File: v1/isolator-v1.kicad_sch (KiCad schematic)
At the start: 43 parts, among them J1 HOST, J2 PORT, Q1 2N7002, T1 750313638, U1 ADuM4165, U2 USBLC6-2SC6, U3 USBLC6-2SC6, U4 SN6505BDBV, U5 TLV76750DGNR, U6 TPS2553DBV, Y1 24M 8pF

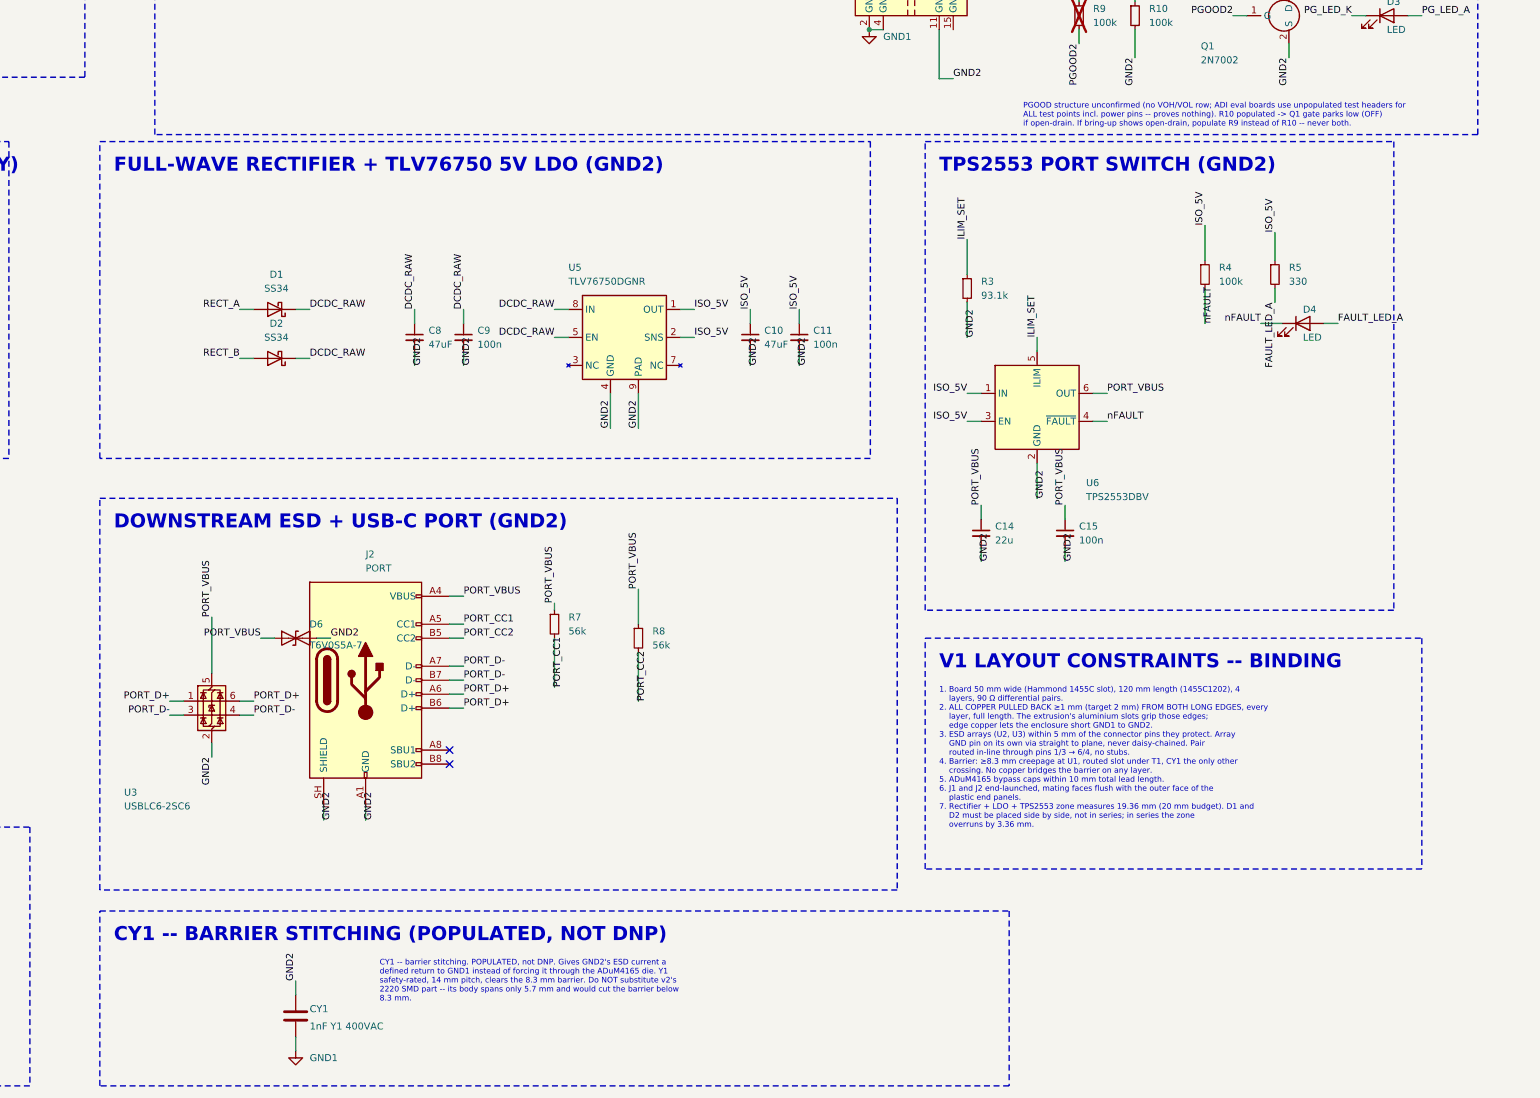
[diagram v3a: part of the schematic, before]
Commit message: fix(v1): final whole-branch review fix wave — R3/FAULT docs, ADuM4165 GND-pin bypass trap, VBUS_HOST cap placement, PGOOD push-pull, title block
Applies all findings from the final whole-branch review
(docs/superpowers/reviews/2026-07-28-v1-schematic-review.md, "Fix round 2"):

Important:
- Corrects the spec's power-budget claim about R3/TPS2553 ILIM. R3 is kept
  unchanged (93.1 kOhm); the documentation now states I_OS = 252/286/324 mA
  min/nom/max (SLVS841F Eq. 1), that the DC-DC's own ~240 mA droop -- not the
  TPS2553 -- is the real port ceiling, that R3's job is soft-start plus a
  short-circuit backstop, and that FAULT will not light on a normal overload
  as an accepted consequence. Mirrored into the spec's verification plan and
  the review record's bring-up notes.
- Adds a new binding layout-constraint item: ADuM4165 U1 pins 4, 7 (GND1)
  and 15, 16, 17 (GND2) are ground-only and not suitable for bypass
  capacitance (datasheet Table 12, p.12); bypass returns must use pins
  2/10 (GND1) or 11/19 (GND2) instead.
- Gives C3, C4, C6, C7 (all on VBUS_HOST) specific Description properties
  naming which IC each bypasses and where it must be placed, verified
  against the SN6505B datasheet (Table 5-1, Sec 10) and the ADuM4165's own
  10 mm bypass-lead budget; adds a matching layout-constraint item.

Minor:
- Reconciles the spec's two DCDC_RAW figures (6.15 V unloaded vs. ~5.8 V
  full load).
- Notes 85% converter efficiency drops the port figure to ~226 mA; 240 mA
  is documented as a best case, not a floor.
- Adds a VDD2-only pull-up warning to the PGOOD schematic note, citing
  PGOOD's VDD2 + 0.5 V absolute maximum (Table 8, p.10).
- Fills in the previously-empty title block (title, date, rev). No
  company/author precedent exists in either project, so those stay blank.

Also records that PGOOD is confirmed push-pull (Table 18, p.15) in both the
review record and the schematic note. R10 stays populated and R9 stays DNP,
unchanged; R10 removal is recorded as an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
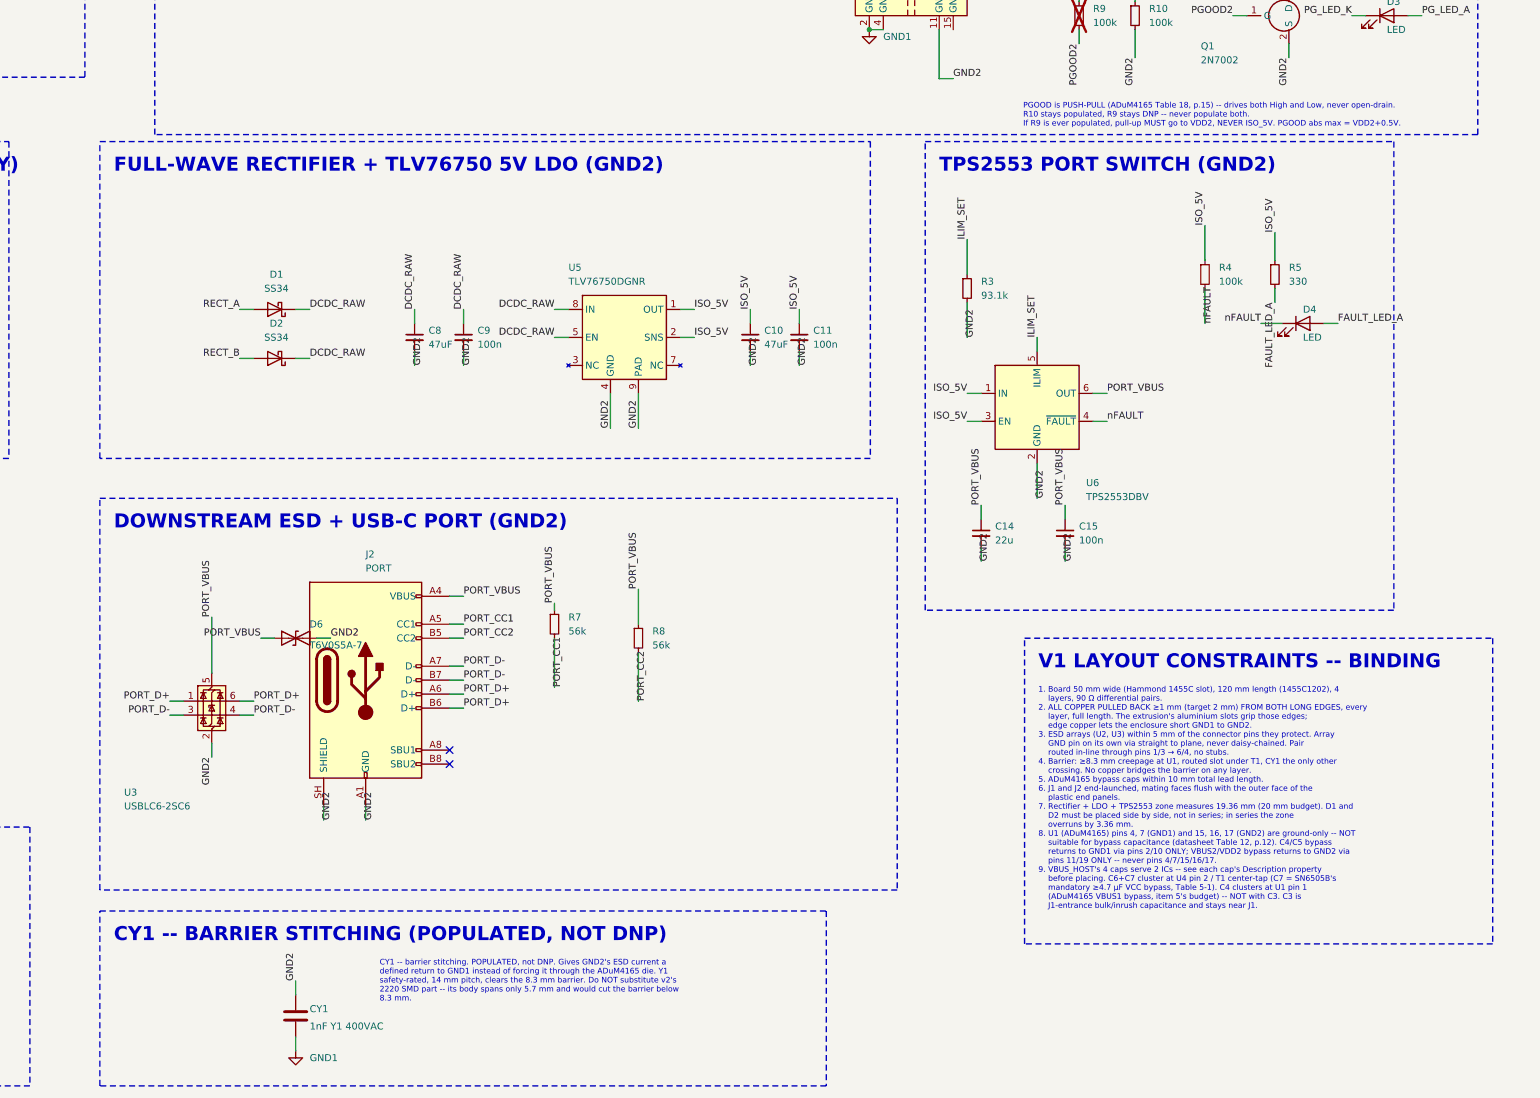
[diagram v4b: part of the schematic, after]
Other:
- note added: "PGOOD is PUSH-PULL (ADuM4165 Table 18, p.15) -- drives both High and Low, never open-drain. R10 stays populated, R9 stays DNP -- never populate both. If R9 is ever populated, pull-up MUST go to VDD2, NEVER ISO_5V. PGOOD abs max = VDD2+0.5V."
- note removed: "PGOOD structure unconfirmed (no VOH/VOL row; ADI eval boards use unpopulated test headers for ALL test points incl. power pins -- proves nothing). R10 populated -> Q1 gate parks low (OFF) if open-drain. If bring-up shows open-drain, populate R9 instead of R10 -- never both."
- title: (none) -> Isolated USB 2.0 Cable — v1
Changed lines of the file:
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@@
 	(generator_version "10.0")
 	(paper "A3")
+	(title_block
+		(title "Isolated USB 2.0 Cable — v1")
+		(date "2026-07-30")
+		(rev "v1.0")
+	)
 	(symbol
 		(lib_id "Device:D_TVS")
@@
 			)
 		)
-		(property "Description" "Unpolarized capacitor, small symbol"
+		(property "Description" "VBUS_HOST bulk/inrush cap at J1 entrance (SN6505B Sec 9.2.2.4 permits supply-entrance placement on a 4-layer board). NOT the SN6505B VCC bypass -- see C7. Layout: place near J1."
 			(at 25.4 49.53 0)
 			(hide yes)
@@
 			)
 		)
-		(property "Description" "Unpolarized capacitor, small symbol"
+		(property "Description" "ADuM4165 U1 VBUS1 mandatory 0.1uF bypass to GND1 (datasheet Table 12, pin 1). Layout: MUST cluster within U1's 10 mm bypass-lead budget at U1 pin 1 -- do NOT leave with C3 near J1."
 			(at 40.64 49.53 0)
 			(hide yes)
@@
 			)
 		)
-		(property "Description" "Unpolarized capacitor, small symbol"
+		(property "Description" "SN6505B U4 VCC close-to-pin bypass, 0.1uF (datasheet Sec 10, Power Supply Recommendations). Layout: place immediately at U4 pin 2 / T1 center-tap, alongside C7."
 			(at 25.4 130.81 0)
 		(hide yes)
@@
 			)
 		)
-		(property "Description" "Unpolarized capacitor, small symbol"
+		(property "Description" "SN6505B U4 VCC mandatory bypass, >=4.7uF low-ESR (datasheet Table 5-1). Layout: place close to U4 pin 2 / T1 center-tap, NOT near J1."
 			(at 38.1 130.81 0)
 		(hide yes)
@@
 		)
 	)
-	(text "PGOOD structure unconfirmed (no VOH/VOL row; ADI eval boards use unpopulated test headers for\nALL test points incl. power pins -- proves nothing). R10 populated -> Q1 gate parks low (OFF)\nif open-drain. If bring-up shows open-drain, populate R9 instead of R10 -- never both."
+	(text "PGOOD is PUSH-PULL (ADuM4165 Table 18, p.15) -- drives both High and Low, never open-drain.\nR10 stays populated, R9 stays DNP -- never populate both.\nIf R9 is ever populated, pull-up MUST go to VDD2, NEVER ISO_5V. PGOOD abs max = VDD2+0.5V."
 		(exclude_from_sim no)
 		(at 332.74 97.79 0)
@@
 	(rectangle
 		(start 165.1 240.03)
-		(end 330.2 271.78)
+		(end 297.0 271.78)
 		(stroke
 			(width 0.254)
@@
 	)
 	(rectangle
-		(start 314.96 190.5)
-		(end 405.13 232.41)
+		(start 333.0 190.5)
+		(end 418.0 246.0)
 		(stroke
 			(width 0.254)
@@
 	(text "V1 LAYOUT CONSTRAINTS -- BINDING"
 		(exclude_from_sim no)
-		(at 317.5 196.34 0)
+		(at 335.5 196.34 0)
 		(effects
 			(font
@@
 		)
 	)
-	(text "1. Board 50 mm wide (Hammond 1455C slot), 120 mm length (1455C1202), 4\n    layers, 90 Ω differential pairs.\n2. ALL COPPER PULLED BACK ≥1 mm (target 2 mm) FROM BOTH LONG EDGES, every\n    layer, full length. The extrusion's aluminium slots grip those edges;\n    edge copper lets the enclosure short GND1 to GND2.\n3. ESD arrays (U2, U3) within 5 mm of the connector pins they protect. Array\n    GND pin on its own via straight to plane, never daisy-chained. Pair\n    routed in-line through pins 1/3 → 6/4, no stubs.\n4. Barrier: ≥8.3 mm creepage at U1, routed slot under T1, CY1 the only other\n    crossing. No copper bridges the barrier on any layer.\n5. ADuM4165 bypass caps within 10 mm total lead length.\n6. J1 and J2 end-launched, mating faces flush with the outer face of the\n    plastic end panels.\n7. Rectifier + LDO + TPS2553 zone measures 19.36 mm (20 mm budget). D1 and\n    D2 must be placed side by side, not in series; in series the zone\n    overruns by 3.36 mm."
+	(text "1. Board 50 mm wide (Hammond 1455C slot), 120 mm length (1455C1202), 4\n    layers, 90 Ω differential pairs.\n2. ALL COPPER PULLED BACK ≥1 mm (target 2 mm) FROM BOTH LONG EDGES, every\n    layer, full length. The extrusion's aluminium slots grip those edges;\n    edge copper lets the enclosure short GND1 to GND2.\n3. ESD arrays (U2, U3) within 5 mm of the connector pins they protect. Array\n    GND pin on its own via straight to plane, never daisy-chained. Pair\n    routed in-line through pins 1/3 → 6/4, no stubs.\n4. Barrier: ≥8.3 mm creepage at U1, routed slot under T1, CY1 the only other\n    crossing. No copper bridges the barrier on any layer.\n5. ADuM4165 bypass caps within 10 mm total lead length.\n6. J1 and J2 end-launched, mating faces flush with the outer face of the\n    plastic end panels.\n7. Rectifier + LDO + TPS2553 zone measures 19.36 mm (20 mm budget). D1 and\n    D2 must be placed side by side, not in series; in series the zone\n    overruns by 3.36 mm.\n8. U1 (ADuM4165) pins 4, 7 (GND1) and 15, 16, 17 (GND2) are ground-only -- NOT\n    suitable for bypass capacitance (datasheet Table 12, p.12). C4/C5 bypass\n    returns to GND1 via pins 2/10 ONLY; VBUS2/VDD2 bypass returns to GND2 via\n    pins 11/19 ONLY -- never pins 4/7/15/16/17.\n9. VBUS_HOST's 4 caps serve 2 ICs -- see each cap's Description property\n    before placing. C6+C7 cluster at U4 pin 2 / T1 center-tap (C7 = SN6505B's\n    mandatory ≥4.7 µF VCC bypass, Table 5-1). C4 clusters at U1 pin 1\n    (ADuM4165 VBUS1 bypass, item 5's budget) -- NOT with C3. C3 is\n    J1-entrance bulk/inrush capacitance and stays near J1."
 		(exclude_from_sim no)
-		(at 317.5 199.39 0)
+		(at 335.5 199.39 0)
 		(effects
 			(font
